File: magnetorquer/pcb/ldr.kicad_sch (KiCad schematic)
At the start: 1 part

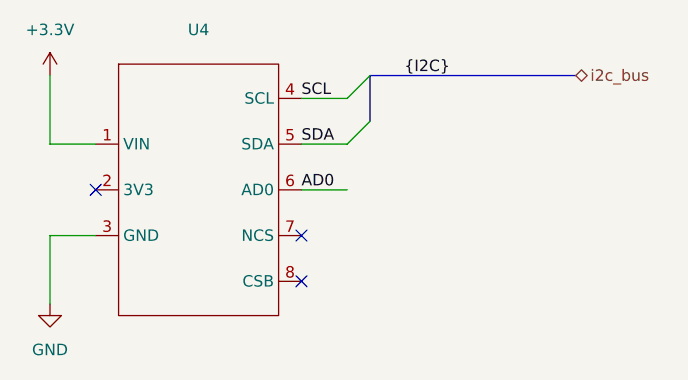
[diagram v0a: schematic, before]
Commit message: feat: lilygo s3 sch/footprint clean up sch
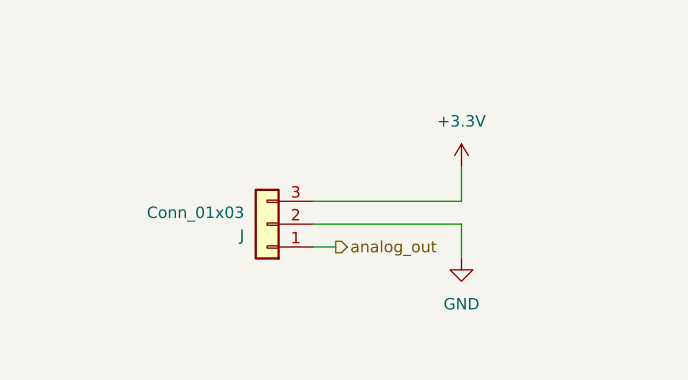
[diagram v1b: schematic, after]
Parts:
- removed U4: ~, custom:GY-91, symbol custom:GY-91
- added J: Conn_01x03, Connector_PinHeader_2.54mm:PinHeader_1x03_P2.54mm_Vertical, symbol Connector_Generic:Conn_01x03
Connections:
- net +3.3V: now also J.3 (Pin_3)
- net GND: now also J.2 (Pin_2)
- new net analog_out: J.1 (Pin_1)
- no-connect marks 3 -> 0
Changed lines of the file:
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@@
 	(generator_version "9.0")
 	(paper "A4")
-	(bus_alias "I2C"
-		(members "SDA" "SCL")
-	)
-	(no_connect
-		(at 138.43 82.55)
-	)
-	(no_connect
-		(at 115.57 72.39)
-	)
-	(no_connect
-		(at 138.43 77.47)
-	)
-	(bus_entry
-		(at 146.05 64.77)
-		(size -2.54 2.54)
-		(stroke
-			(width 0)
-			(type default)
-		)
-	)
-	(bus_entry
-		(at 146.05 59.69)
-		(size -2.54 2.54)
-		(stroke
-			(width 0)
-			(type default)
-		)
-	)
-	(wire
-		(pts
-			(xy 110.49 67.31) (xy 115.57 67.31)
-		)
-		(stroke
-			(width 0)
-			(type default)
-		)
-	)
-	(bus
-		(pts
-			(xy 146.05 59.69) (xy 146.05 64.77)
-		)
-		(stroke
-			(width 0)
-			(type default)
-		)
-	)
-	(wire
-		(pts
-			(xy 143.51 62.23) (xy 138.43 62.23)
-		)
-		(stroke
-			(width 0)
-			(type default)
-		)
-	)
-	(bus
-		(pts
-			(xy 146.05 59.69) (xy 168.91 59.69)
-		)
-		(stroke
-			(width 0)
-			(type default)
-		)
-	)
-	(wire
-		(pts
-			(xy 110.49 59.69) (xy 110.49 67.31)
-		)
-		(stroke
-			(width 0)
-			(type default)
-		)
-	)
-	(wire
-		(pts
-			(xy 143.51 67.31) (xy 138.43 67.31)
-		)
-		(stroke
-			(width 0)
-			(type default)
-		)
-	)
-	(wire
-		(pts
-			(xy 138.43 72.39) (xy 143.51 72.39)
-		)
-		(stroke
-			(width 0)
-			(type default)
-		)
-	)
-	(wire
-		(pts
-			(xy 110.49 77.47) (xy 110.49 85.09)
-		)
-		(stroke
-			(width 0)
-			(type default)
-		)
-	)
-	(wire
-		(pts
-			(xy 115.57 77.47) (xy 110.49 77.47)
-		)
-		(stroke
-			(width 0)
-			(type default)
-		)
-	)
-	(label "AD0"
-		(at 138.43 72.39 0)
+	(wire
+		(pts
+			(xy 156.21 76.2) (xy 156.21 80.01)
+		)
+		(stroke
+			(width 0)
+			(type default)
+		)
+	)
+	(wire
+		(pts
+			(xy 139.7 73.66) (xy 156.21 73.66)
+		)
+		(stroke
+			(width 0)
+			(type default)
+		)
+	)
+	(wire
+		(pts
+			(xy 156.21 73.66) (xy 156.21 69.85)
+		)
+		(stroke
+			(width 0)
+			(type default)
+		)
+	)
+	(wire
+		(pts
+			(xy 139.7 76.2) (xy 156.21 76.2)
+		)
+		(stroke
+			(width 0)
+			(type default)
+		)
+	)
+	(wire
+		(pts
+			(xy 142.24 78.74) (xy 139.7 78.74)
+		)
+		(stroke
+			(width 0)
+			(type default)
+		)
+	)
+	(hierarchical_label "analog_out"
+		(shape output)
+		(at 142.24 78.74 0)
 		(effects
 			(font
 				(size 1.27 1.27)
 			)
-			(justify left bottom)
-		)
-	)
-	(label "SDA"
-		(at 138.43 67.31 0)
-		(effects
-			(font
-				(size 1.27 1.27)
-			)
-			(justify left bottom)
-		)
-	)
-	(label "SCL"
-		(at 138.43 62.23 0)
-		(effects
-			(font
-				(size 1.27 1.27)
-			)
-			(justify left bottom)
-		)
-	)
-	(label "{I2C}"
-		(at 149.86 59.69 0)
-		(effects
-			(font
-				(size 1.27 1.27)
-			)
-			(justify left bottom)
-		)
-	)
-	(hierarchical_label "i2c_bus"
-		(shape bidirectional)
-		(at 168.91 59.69 0)
-		(effects
-			(font
-				(size 1.27 1.27)
-			)
 			(justify left)
 		)
 	)
 	(symbol
-		(lib_id "custom:GY-91")
-		(at 127 72.39 0)
+		(lib_id "Connector_Generic:Conn_01x03")
+		(at 134.62 76.2 180)
 		(unit 1)
 		(exclude_from_sim no)
@@
 		(dnp no)
 		(fields_autoplaced yes)
-		(property "Reference" "U4"
-			(at 127 54.61 0)
-			(effects
-				(font
-					(size 1.27 1.27)
-				)
-			)
-		)
-		(property "Value" "~"
-			(at 127 57.15 0)
-			(effects
-				(font
-					(size 1.27 1.27)
-				)
-			)
-		)
-		(property "Footprint" "custom:GY-91"
-			(at 127.508 55.118 0)
-			(effects
-				(font
-					(size 1.27 1.27)
-				)
-				(hide yes)
-			)
-		)
-		(property "Datasheet" "https://github.com/ricardozago/GY91-MPU9250-BMP280/blob/master/Datasheet/ak8963c-datasheet.pdf"
-			(at 127.508 91.44 0)
-			(effects
-				(font
-					(size 1.27 1.27)
-				)
-				(hide yes)
-			)
-		)
-		(property "Description" "10 in 1: acc, mag, gyro, barometer: i2c, spi"
-			(at 127.254 88.138 0)
-			(effects
-				(font
-					(size 1.27 1.27)
-				)
-				(hide yes)
-			)
-		)
-		(pin "4"
-		)
-		(pin "7"
-		)
-		(pin "5"
-		)
-		(pin "6"
-		)
-		(pin "8"
+		(property "Reference" "J"
+			(at 132.08 77.4701 0)
+			(effects
+				(font
+					(size 1.27 1.27)
+				)
+				(justify left)
+			)
+		)
+		(property "Value" "Conn_01x03"
+			(at 132.08 74.9301 0)
+			(effects
+				(font
+					(size 1.27 1.27)
+				)
+				(justify left)
+			)
+		)
+		(property "Footprint" "Connector_PinHeader_2.54mm:PinHeader_1x03_P2.54mm_Vertical"
+			(at 134.62 76.2 0)
+			(effects
+				(font
+					(size 1.27 1.27)
+				)
+				(hide yes)
+			)
+		)
+		(property "Datasheet" "~"
+			(at 134.62 76.2 0)
+			(effects
+				(font
+					(size 1.27 1.27)
+				)
+				(hide yes)
+			)
+		)
+		(property "Description" "Generic connector, single row, 01x03, script generated (kicad-library-utils/schlib/autogen/connector/)"
+			(at 134.62 76.2 0)
+			(effects
+				(font
+					(size 1.27 1.27)
+				)
+				(hide yes)
+			)
 		)
 		(pin "3"
 		)
+		(pin "1"
+		)
 		(pin "2"
 		)
-		(pin "1"
+		(instances
+			(project "mag"
+				(path "/14c04de7-71ee-4f20-9e6e-041dbb035733/15af55bb-e28b-4539-9b7d-24d137fdf430"
+					(reference "J4")
+					(unit 1)
+				)
+				(path "/14c04de7-71ee-4f20-9e6e-041dbb035733/9f990fc4-e861-4ed4-b802-8259016bf14d"
+					(reference "J5")
+					(unit 1)
+				)
+				(path "/14c04de7-71ee-4f20-9e6e-041dbb035733/f90e8bbb-8262-4c4d-81f6-93d124f86469"
+					(reference "J6")
+					(unit 1)
+				)
+			)
 		)
 	)
 	(symbol
 		(lib_id "power:GND")
-		(at 110.49 85.09 0)
+		(at 156.21 80.01 0)
 		(unit 1)
 		(exclude_from_sim no)
@@
 		(dnp no)
 		(fields_autoplaced yes)
-		(property "Reference" "#PWR018"
-			(at 110.49 91.44 0)
+		(property "Reference" "#PWR"
+			(at 156.21 86.36 0)
 			(effects
 				(font
@@
 		)
 		(property "Value" "GND"
-			(at 110.49 90.17 0)
+			(at 156.21 85.09 0)
 			(effects
 				(font
@@
 		)
 		(property "Footprint" ""
-			(at 110.49 85.09 0)
+			(at 156.21 80.01 0)
 			(effects
 				(font
@@
 		)
 		(property "Datasheet" ""
-			(at 110.49 85.09 0)
+			(at 156.21 80.01 0)
 			(effects
 				(font
@@
 		)
 		(property "Description" "Power symbol creates a global label with name \"GND\" , ground"
-			(at 110.49 85.09 0)
+			(at 156.21 80.01 0)
 			(effects
 				(font
@@
 		)
 		(pin "1"
+		)
+		(instances
+			(project "mag"
+				(path "/14c04de7-71ee-4f20-9e6e-041dbb035733/15af55bb-e28b-4539-9b7d-24d137fdf430"
+					(reference "#PWR020")
+					(unit 1)
+				)
+				(path "/14c04de7-71ee-4f20-9e6e-041dbb035733/9f990fc4-e861-4ed4-b802-8259016bf14d"
+					(reference "#PWR022")
+					(unit 1)
+				)
+				(path "/14c04de7-71ee-4f20-9e6e-041dbb035733/f90e8bbb-8262-4c4d-81f6-93d124f86469"
+					(reference "#PWR024")
+					(unit 1)
+				)
+			)
 		)
 	)
 	(symbol
 		(lib_id "power:+3.3V")
-		(at 110.49 59.69 0)
+		(at 156.21 69.85 0)
 		(unit 1)
 		(exclude_from_sim no)
@@
 		(dnp no)
 		(fields_autoplaced yes)
-		(property "Reference" "#PWR016"
-			(at 110.49 63.5 0)
+		(property "Reference" "#PWR"
+			(at 156.21 73.66 0)
 			(effects
 				(font
@@
 		)
 		(property "Value" "+3.3V"
-			(at 110.49 54.61 0)
+			(at 156.21 64.77 0)
 			(effects
 				(font
@@
 		)
 		(property "Footprint" ""
-			(at 110.49 59.69 0)
+			(at 156.21 69.85 0)
 			(effects
 				(font
@@
 		)
 		(property "Datasheet" ""
-			(at 110.49 59.69 0)
+			(at 156.21 69.85 0)
 			(effects
 				(font
@@
 		)
 		(property "Description" "Power symbol creates a global label with name \"+3.3V\""
-			(at 110.49 59.69 0)
+			(at 156.21 69.85 0)
 			(effects
 				(font
@@
 		(pin "1"
 		)
-	)
+		(instances
+			(project "mag"
+				(path "/14c04de7-71ee-4f20-9e6e-041dbb035733/15af55bb-e28b-4539-9b7d-24d137fdf430"
+					(reference "#PWR019")
+					(unit 1)
+				)
+				(path "/14c04de7-71ee-4f20-9e6e-041dbb035733/9f990fc4-e861-4ed4-b802-8259016bf14d"
+					(reference "#PWR021")
+					(unit 1)
+				)
+				(path "/14c04de7-71ee-4f20-9e6e-041dbb035733/f90e8bbb-8262-4c4d-81f6-93d124f86469"
+					(reference "#PWR023")
+					(unit 1)
+				)
+			)
+		)
+	)

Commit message: feat: upload all changes for sch
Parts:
- renumbered J to J3
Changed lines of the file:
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@@
 		(dnp no)
 		(fields_autoplaced yes)
-		(property "Reference" "J"
+		(property "Reference" "J3"
 			(at 132.08 77.4701 0)
 			(effects
@@
 				(path "/14c04de7-71ee-4f20-9e6e-041dbb035733/15af55bb-e28b-4539-9b7d-24d137fdf430"
 					(reference "J4")
+					(unit 1)
+				)
+				(path "/14c04de7-71ee-4f20-9e6e-041dbb035733/714785ba-3303-4d57-9c32-4841bec1e1c2"
+					(reference "J3")
 					(unit 1)
 				)
@@
 		(dnp no)
 		(fields_autoplaced yes)
-		(property "Reference" "#PWR"
+		(property "Reference" "#PWR0103"
 			(at 156.21 86.36 0)
 			(effects
@@
 				(path "/14c04de7-71ee-4f20-9e6e-041dbb035733/15af55bb-e28b-4539-9b7d-24d137fdf430"
 					(reference "#PWR020")
+					(unit 1)
+				)
+				(path "/14c04de7-71ee-4f20-9e6e-041dbb035733/714785ba-3303-4d57-9c32-4841bec1e1c2"
+					(reference "#PWR0103")
 					(unit 1)
 				)
@@
 		(dnp no)
 		(fields_autoplaced yes)
-		(property "Reference" "#PWR"
+		(property "Reference" "#PWR0104"
 			(at 156.21 73.66 0)
 			(effects
@@
 					(unit 1)
 				)
+				(path "/14c04de7-71ee-4f20-9e6e-041dbb035733/714785ba-3303-4d57-9c32-4841bec1e1c2"
+					(reference "#PWR0104")
+					(unit 1)
+				)
